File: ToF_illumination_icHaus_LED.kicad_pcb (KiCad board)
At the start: 2 copper layers, 50 x 50 mm, 41 parts, among them J1 Screw_Terminal_01x02, J2 Conn_01x10, J3 Conn_01x02, J4 Conn_01x02, U1 SN74AUP1T34DCK, U2 MCP1541-TT, U3 iC-HGP, U4 LM2937xT

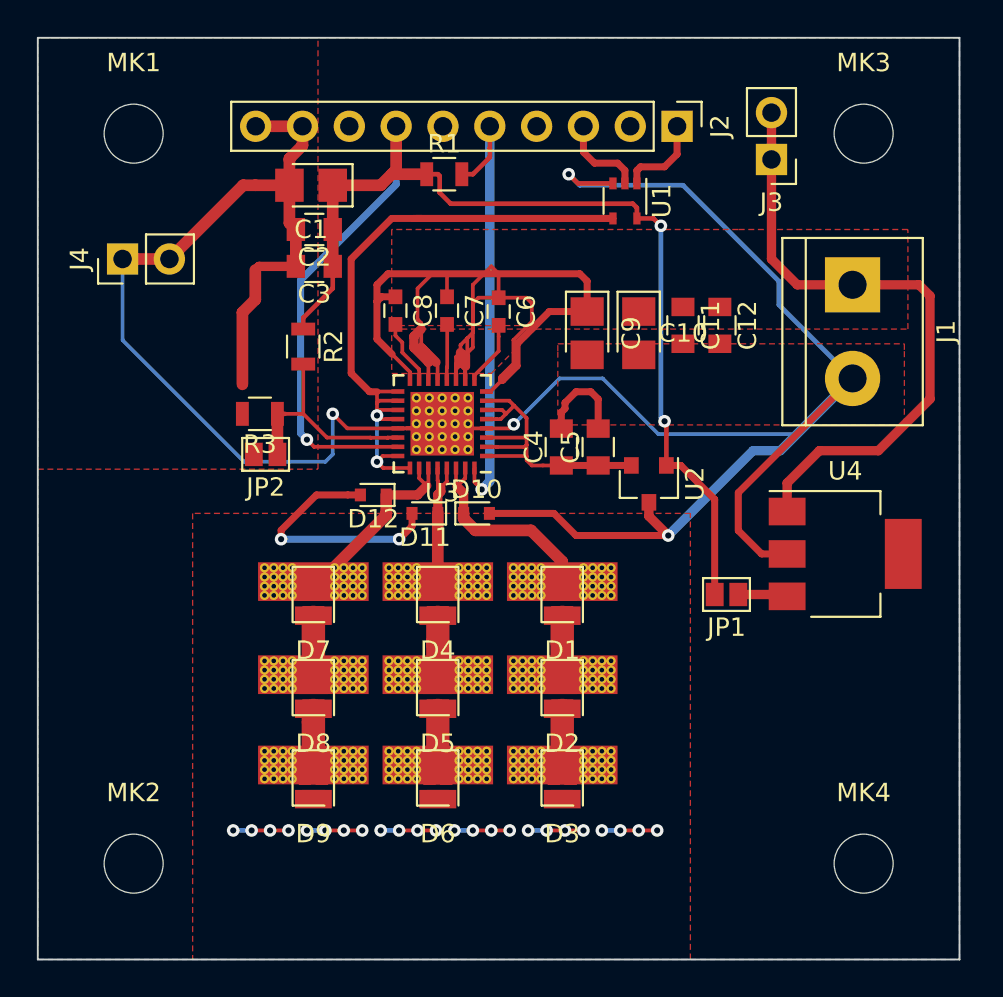
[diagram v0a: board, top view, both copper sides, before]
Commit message: Tantalum capacitors were changed to 1210 size and project was moved to KiCad 5.1.4
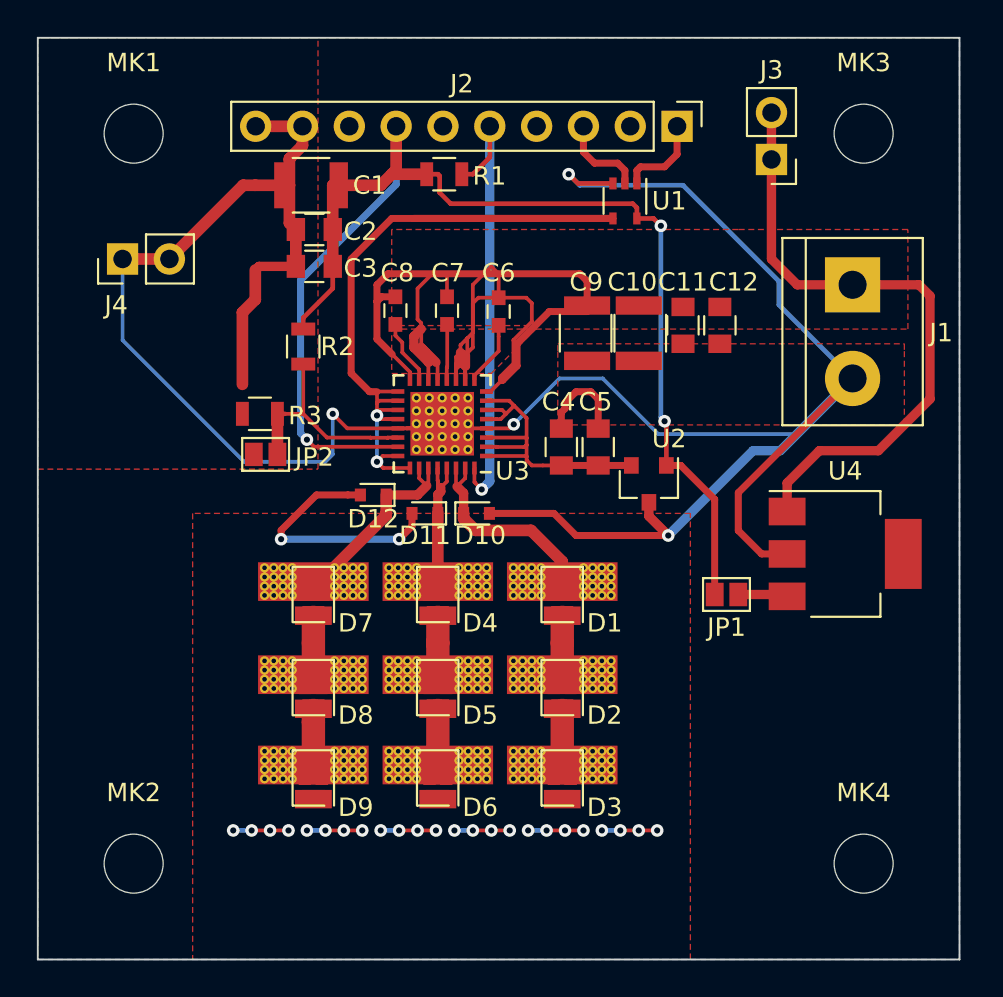
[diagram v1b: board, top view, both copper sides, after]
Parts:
- C1, C10, C9: footprint Capacitors_Tantalum_SMD:CP_Tantalum_Case-R_EIA-2012-12_Reflow -> Capacitors_SMD:C_1210
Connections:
- J2 pad 2: Net-(J2-Pad2) -> (no net)
- J2 pad 4: Net-(J2-Pad4) -> (no net)
- J2 pad 6: Net-(J2-Pad6) -> (no net)
- J2 pad 8: Net-(J2-Pad8) -> (no net)
- MK1 pad 1: Net-(MK1-Pad1) -> (no net)
- MK2 pad 1: Net-(MK2-Pad1) -> (no net)
- MK3 pad 1: Net-(MK3-Pad1) -> (no net)
- MK4 pad 1: Net-(MK4-Pad1) -> (no net)

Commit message: Added BOM, improved footprints a bit.
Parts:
- C6, C7, C8: footprint Capacitors_SMD:C_0603 -> Capacitors_SMD:C_0805
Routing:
- net +12V: track 103.7 -> 80.2 mm
- net Net-(C8-Pad2): track 3.52 -> 6.54 mm

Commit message: Gerbers added and some labels on the board for assembly added
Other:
- board text added: "+12V"
- board text added: "+5V"
- board text added: "ENABLE"
- board text added: "GND"
- board text added: "NERROR"
- board text added: "VIO"
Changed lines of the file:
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@@
   (general
     (thickness 1.6)
-    (drawings 7)
+    (drawings 15)
     (tracks 379)
     (zones 0)
@@
   )
   (setup
-    (last_trace_width 0.508)
+    (last_trace_width 1.27)
     (user_trace_width 0.1524)
     (user_trace_width 0.2032)
@@
     (add_net "Net-(D7-Pad1)")
     (add_net "Net-(D8-Pad1)")
-    (add_net "Net-(J2-Pad2)")
-    (add_net "Net-(J2-Pad4)")
-    (add_net "Net-(J2-Pad6)")
-    (add_net "Net-(J2-Pad8)")
     (add_net "Net-(JP1-Pad1)")
     (add_net "Net-(JP2-Pad1)")
-    (add_net "Net-(MK1-Pad1)")
-    (add_net "Net-(MK2-Pad1)")
-    (add_net "Net-(MK3-Pad1)")
-    (add_net "Net-(MK4-Pad1)")
     (add_net "Net-(U1-Pad4)")
   )
@@
       (rotate (xyz 0 0 0))
     )
+  )
+  (gr_text +5V (at 119 108) (layer F.Cu)
+    (effects (font (size 1 1) (thickness 0.25)))
+  )
+  (gr_text GND (at 93 76) (layer F.Cu)
+    (effects (font (size 0.5 0.5) (thickness 0.125)))
+  )
+  (gr_text +5V (at 99 77) (layer F.Cu)
+    (effects (font (size 0.5 0.5) (thickness 0.125)))
+  )
+  (gr_text NERROR (at 104 77) (layer F.Cu)
+    (effects (font (size 0.5 0.5) (thickness 0.125)))
+  )
+  (gr_text ENABLE (at 110 77) (layer F.Cu)
+    (effects (font (size 0.5 0.5) (thickness 0.125)))
+  )
+  (gr_text VIO (at 115 77) (layer F.Cu)
+    (effects (font (size 0.5 0.5) (thickness 0.125)))
+  )
+  (gr_text GND (at 82 92 90) (layer F.Cu)
+    (effects (font (size 1.5 1.5) (thickness 0.3)))
+  )
+  (gr_text +12V (at 126 85) (layer F.Cu)
+    (effects (font (size 1.5 1.5) (thickness 0.3)))
   )
   (gr_text "NO CONNECTORS " (at 71 108 90) (layer Dwgs.User)
@@
   (segment (start 106.517911 96.717911) (end 106.517911 97.082089) (width 0.2032) (layer F.Cu) (net 3))
   (segment (start 106.517911 97.082089) (end 106.517911 97.717911) (width 0.2032) (layer F.Cu) (net 3))
-  (segment (start 119.8 79.06) (end 119.8 81.6) (width 0.508) (layer F.Cu) (net 4))
-  (segment (start 121.2 88.4) (end 124.2 88.4) (width 0.508) (layer F.Cu) (net 4))
-  (segment (start 119.8 81.6) (end 119.8 87) (width 0.508) (layer F.Cu) (net 4))
-  (segment (start 119.8 87) (end 121.2 88.4) (width 0.508) (layer F.Cu) (net 4))
   (segment (start 120.65 99.15) (end 120.65 100.7) (width 0.508) (layer F.Cu) (net 4))
   (segment (start 127.8 88.4) (end 128.4 89) (width 0.508) (layer F.Cu) (net 4))
@@
   (segment (start 98 91.9) (end 99.05 92.95) (width 0.508) (layer F.Cu) (net 4))
   (segment (start 99.05 92.95) (end 99.6375 93.5375) (width 0.254) (layer F.Cu) (net 4))
+  (segment (start 119.8 81.6) (end 119.8 86.8) (width 1.27) (layer F.Cu) (net 4))
+  (segment (start 121.4 88.4) (end 124.2 88.4) (width 1.27) (layer F.Cu) (net 4))
+  (segment (start 119.8 86.8) (end 121.4 88.4) (width 1.27) (layer F.Cu) (net 4))
+  (segment (start 119.8 81.6) (end 119.8 79.06) (width 1.27) (layer F.Cu) (net 4))
   (segment (start 103.6875 93.3125) (end 105 92) (width 0.2032) (layer F.Cu) (net 5))
   (segment (start 105 91.2032) (end 105 90.6) (width 0.2032) (layer F.Cu) (net 5))
